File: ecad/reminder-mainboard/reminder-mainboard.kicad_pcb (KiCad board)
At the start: 2 copper layers, 34 parts, among them J1 USB_B_Micro, J2 22-03-5035, J3 22-03-5025, J4 22-03-5065, Q1 2N3904, Q2 2N3904, Q3 2N3904, Q4 2N3904, U1 LM1117-3.3, U2 QRD1113GR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

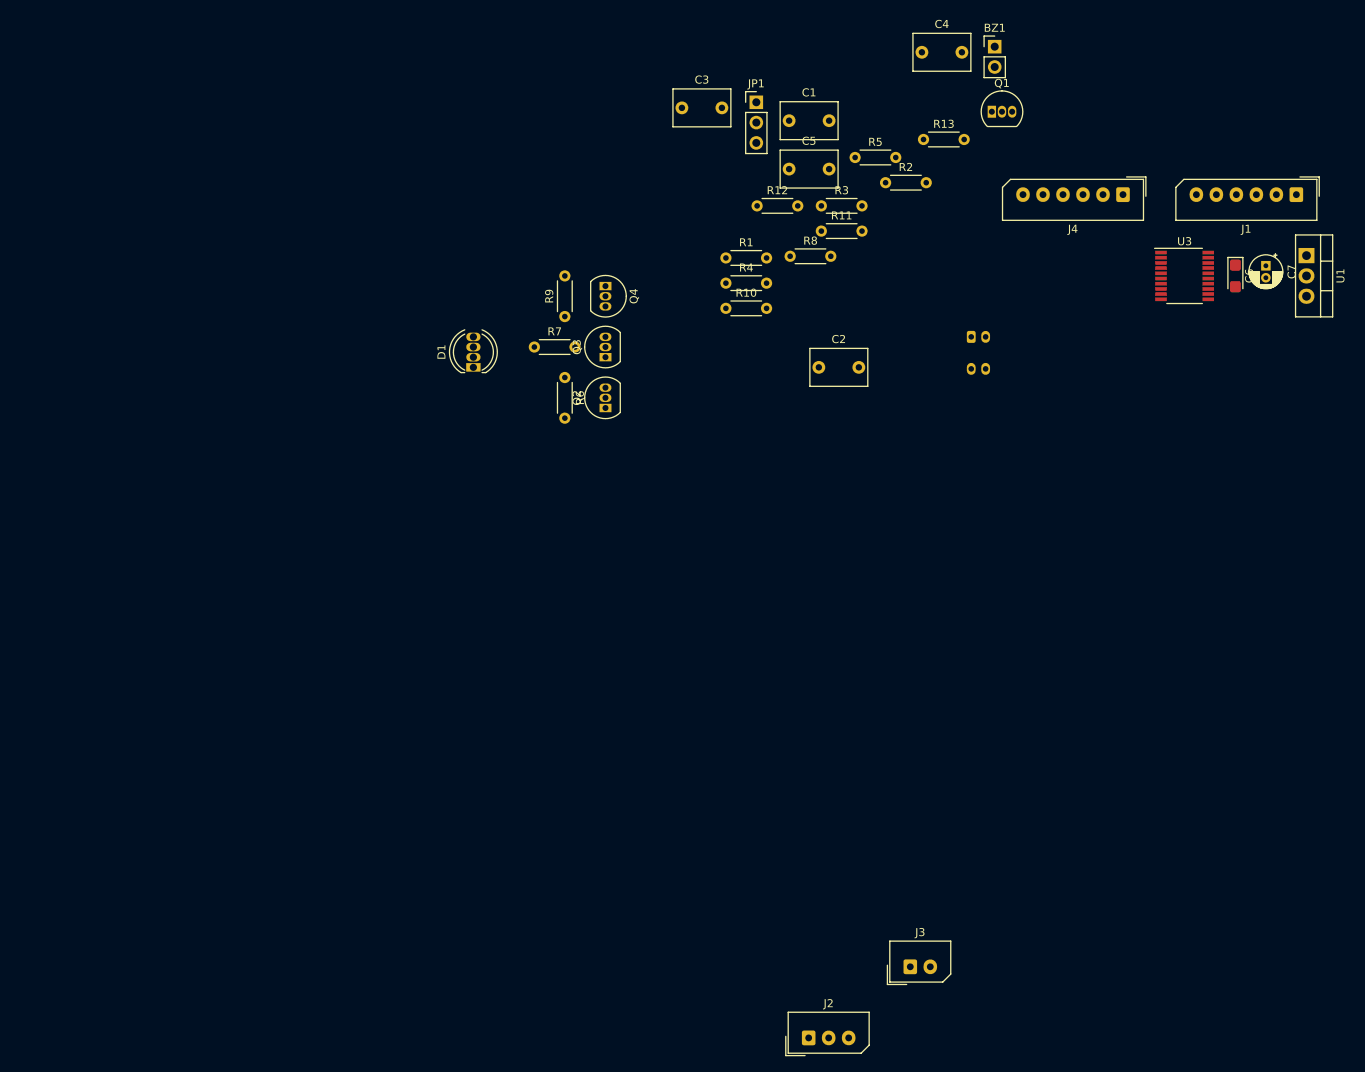
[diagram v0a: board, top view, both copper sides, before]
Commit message: Began SMD layout
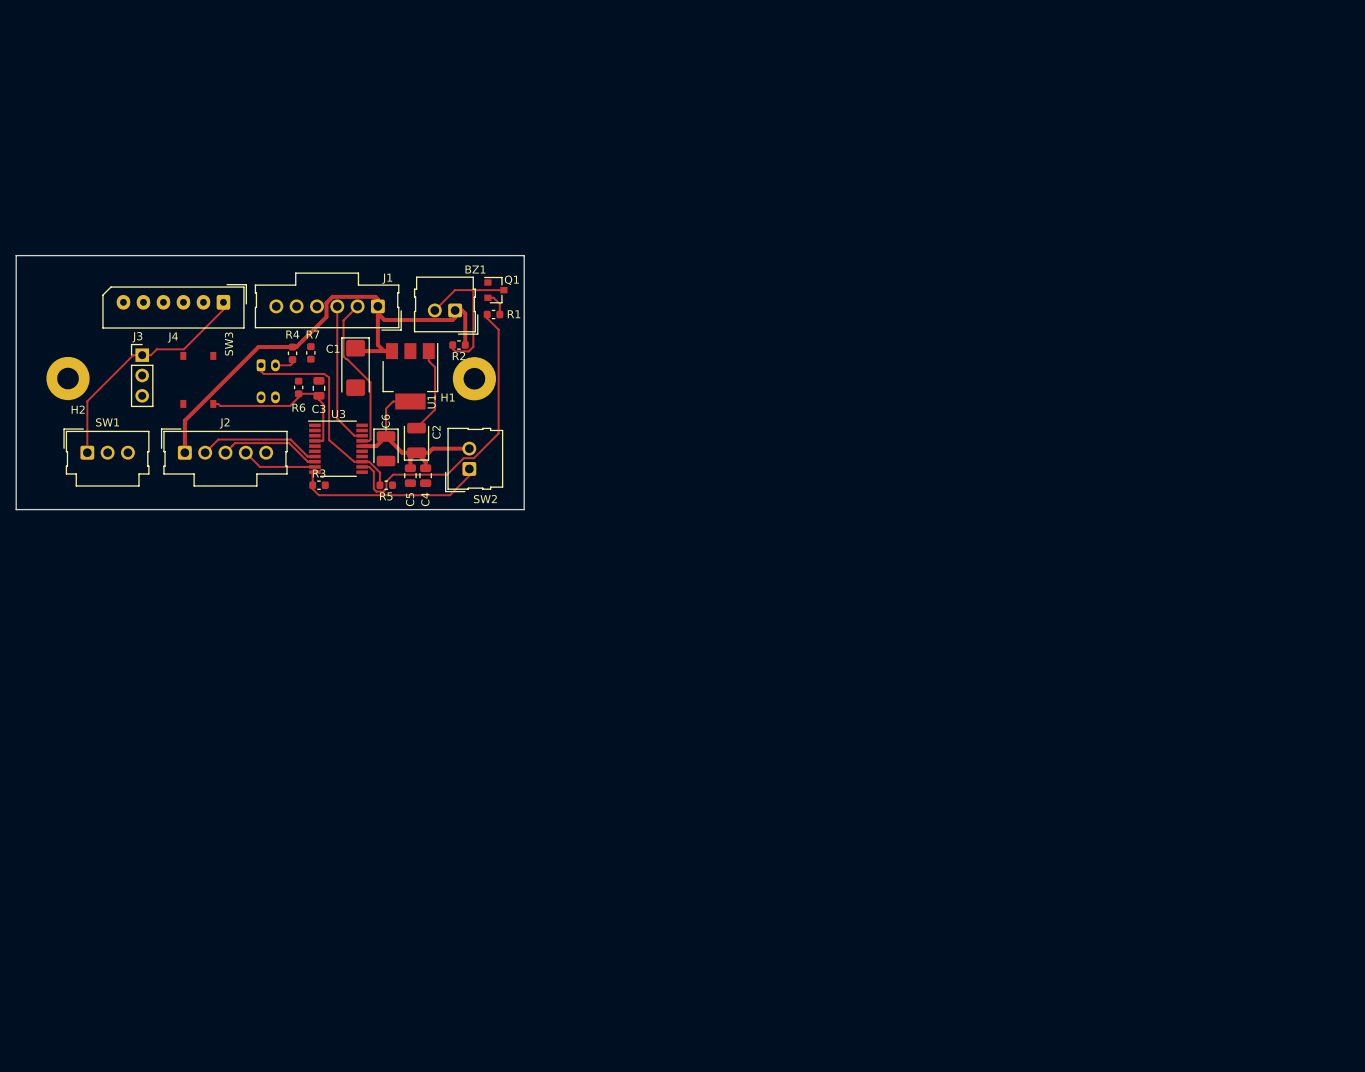
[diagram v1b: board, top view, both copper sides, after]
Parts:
- removed C7: 4.7uF, Capacitor_THT:CP_Radial_D4.0mm_P1.50mm
- removed D1: LED_RGBA, LED_THT:LED_D5.0mm-4_RGB
- removed JP1: Jumper_3_Bridged12, Connector_PinHeader_2.54mm:PinHeader_1x03_P2.54mm_Vertical
- removed Q2, Q3, Q4: 2N3904, Package_TO_SOT_THT:TO-92_Inline
- removed R10: 180, Resistor_THT:R_Axial_DIN0204_L3.6mm_D1.6mm_P5.08mm_Horizontal
- removed R11: 390, Resistor_THT:R_Axial_DIN0204_L3.6mm_D1.6mm_P5.08mm_Horizontal
- removed R12, R13, R8: 10k, Resistor_THT:R_Axial_DIN0204_L3.6mm_D1.6mm_P5.08mm_Horizontal
- removed R9: 91, Resistor_THT:R_Axial_DIN0204_L3.6mm_D1.6mm_P5.08mm_Horizontal
- added H1: MountingHole, MountingHole:MountingHole_2.7mm_M2.5_Pad, F.Cu at (120.8, 110.6)
- added H2: MountingHole, MountingHole:MountingHole_2.7mm_M2.5_Pad, F.Cu at (70.0, 110.6)
- added SW1: SW_SPDT, Connector_Molex:Molex_SL_171971-0003_1x03_P2.54mm_Vertical, F.Cu at (72.4, 119.9)
- added SW2: SW_Push, Connector_Molex:Molex_SL_171971-0002_1x02_P2.54mm_Vertical, F.Cu at (120.1, 121.9)
- added SW3: SW_Push, jlcpcb:TACT_SWITCH_TS-1187A-X-X-X, F.Cu at (88.1, 107.8)
- BZ1: value (none) -> Buzzer; footprint Connector_PinHeader_2.54mm:PinHeader_1x02_P2.54mm_Vertical -> Connector_Molex:Molex_SL_171971-0002_1x02_P2.54mm_Vertical
- C1: footprint Capacitor_THT:C_Rect_L7.0mm_W4.5mm_P5.00mm -> Capacitor_Tantalum_SMD:CP_EIA-6032-28_Kemet-C
- C2: value 10uF -> 100uF; footprint Capacitor_THT:C_Rect_L7.0mm_W4.5mm_P5.00mm -> Capacitor_Tantalum_SMD:CP_EIA-3528-21_Kemet-B
- C3, C4: value 20pF -> 100nF; footprint Capacitor_THT:C_Rect_L7.0mm_W4.5mm_P5.00mm -> Capacitor_SMD:C_0805_2012Metric
- C5: footprint Capacitor_THT:C_Rect_L7.0mm_W4.5mm_P5.00mm -> Capacitor_SMD:C_0805_2012Metric
- C6: value 100nF -> 10uF; footprint Capacitor_Tantalum_SMD:CP_EIA-3216-10_Kemet-I -> Capacitor_Tantalum_SMD:CP_EIA-3528-21_Kemet-B
- J1: footprint Connector_Molex:Molex_SPOX_5267-06A_1x06_P2.50mm_Vertical -> Connector_Molex:Molex_SL_171971-0006_1x06_P2.54mm_Vertical
- J2: value 22-03-5035 -> MOLEX SL 1x5; footprint Connector_Molex:Molex_SPOX_5267-03A_1x03_P2.50mm_Vertical -> Connector_Molex:Molex_SL_171971-0005_1x05_P2.54mm_Vertical
- J3: value 22-03-5025 -> Conn_01x03_Male; footprint Connector_Molex:Molex_SPOX_5267-02A_1x02_P2.50mm_Vertical -> Connector_PinHeader_2.54mm:PinHeader_1x03_P2.54mm_Vertical
- Q1: footprint Package_TO_SOT_THT:TO-92_Inline -> Package_TO_SOT_SMD:SOT-23
- R1: value 620 -> 510; footprint Resistor_THT:R_Axial_DIN0204_L3.6mm_D1.6mm_P5.08mm_Horizontal -> Resistor_SMD:R_0603_1608Metric
- R2: footprint Resistor_THT:R_Axial_DIN0204_L3.6mm_D1.6mm_P5.08mm_Horizontal -> Resistor_SMD:R_0603_1608Metric
- R3, R5: value 620 -> 10k; footprint Resistor_THT:R_Axial_DIN0204_L3.6mm_D1.6mm_P5.08mm_Horizontal -> Resistor_SMD:R_0603_1608Metric
- R4: value 620 -> 160; footprint Resistor_THT:R_Axial_DIN0204_L3.6mm_D1.6mm_P5.08mm_Horizontal -> Resistor_SMD:R_0603_1608Metric
- R6: value 130 -> 10k; footprint Resistor_THT:R_Axial_DIN0204_L3.6mm_D1.6mm_P5.08mm_Horizontal -> Resistor_SMD:R_0603_1608Metric
- R7: value 91 -> 10k; footprint Resistor_THT:R_Axial_DIN0204_L3.6mm_D1.6mm_P5.08mm_Horizontal -> Resistor_SMD:R_0603_1608Metric
- U1: footprint Package_TO_SOT_THT:TO-220-3_Vertical -> Package_TO_SOT_SMD:SOT-223-3_TabPin2
- moved J3 122.7 mm to (79.2, 107.7)
- moved J1 115.7 mm to (108.7, 101.6)
- moved J4 113.2 mm to (89.4, 101.1)
- moved U1 113.0 mm to (112.8, 110.3)
- moved C6 108.3 mm to (109.7, 119.4)
- moved U3 107.9 mm to (103.8, 119.4)
- moved J2 106.9 mm to (84.6, 119.9)
- moved U2 88.8 mm to (94.1, 109.0)
- moved C4 81.5 mm to (114.7, 122.8), turned to 270 degrees
- moved BZ1 75.1 mm to (118.4, 102.1), turned to 180 degrees
- moved R3 71.9 mm to (101.3, 124.0)
- moved R5 71.5 mm to (109.8, 124.0), turned to 180 degrees
- moved Q1 65.9 mm to (123.5, 99.6)
- moved C1 62.4 mm to (105.9, 109.3), turned to 270 degrees
- moved C5 60.9 mm to (112.8, 122.8), turned to 270 degrees
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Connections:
- C3 pad 1: Net-(C3-Pad1) -> /NRST
- C4 pad 1: Net-(C4-Pad1) -> +3V3
- C5 pad 1: /NRST -> +3V3
- J2 pad 1: +3V3 -> +5V
- J2 pad 2: /MUTE -> /LED_R
- J2 pad 3: GND -> /LED_G
- J3 pad 2: /UI_BUTTON -> Net-(J3-Pad2)
- R3 pad 1: /LED_R -> /UI_BUTTON
- R3 pad 2: Net-(Q2-Pad2) -> GND
- R4 pad 1: /LED_G -> +5V
- R4 pad 2: Net-(Q3-Pad2) -> Net-(R4-Pad2)
- R5 pad 1: /LED_B -> +3V3
- R5 pad 2: Net-(Q4-Pad2) -> /SENSOR
- R6 pad 1: Net-(D1-Pad1) -> +3V3
- R6 pad 2: Net-(Q2-Pad3) -> /NRST
- R7 pad 1: Net-(D1-Pad2) -> Net-(R7-Pad1)
- R7 pad 2: Net-(Q3-Pad3) -> Net-(J3-Pad2)
- U2 pad 3: Net-(R10-Pad2) -> Net-(R4-Pad2)
- U3 pad 1: Net-(R13-Pad1) -> Net-(R7-Pad1)
- U3 pad 2: Net-(C3-Pad1) -> (no net)
- U3 pad 3: Net-(R11-Pad1) -> (no net)
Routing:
- net +5V: track 0.00 -> 65.4 mm
- net +3V3: track 0.00 -> 55.6 mm
- net /BUZZER: track 0.00 -> 38.6 mm
- net /SENSOR: track 0.00 -> 26.9 mm
- net /UI_BUTTON: track 0.00 -> 24.0 mm
- net /NRST: track 0.00 -> 21.2 mm
- net Net-(BZ1-Pad2): track 0.00 -> 20.2 mm
- net /USB_M: track 0.00 -> 20.0 mm
- net /USB_P: track 0.00 -> 18.0 mm
- net /LED_R: track 0.00 -> 15.3 mm
- net /LED_G: track 0.00 -> 12.6 mm
- net GND: track 0.00 -> 10.9 mm
- net /LED_B: track 0.00 -> 9.37 mm
- net Net-(Q1-Pad2): track 0.00 -> 3.13 mm
- net Net-(R4-Pad2): track 0.00 -> 2.69 mm
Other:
- board outline added: 63.5 x 31.8 mm

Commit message: Finished routing
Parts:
- moved R5 5.11 mm to (104.6, 124.0), turned to 0 degrees
- moved R3 1.06 mm to (100.6, 124.7), turned to 270 degrees
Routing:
- net +3V3: track 55.6 -> 101.8 mm, vias 0 -> 2
- net /SWDIO: track 0.00 -> 38.1 mm, vias 0 -> 1
- net /MUTE: track 0.00 -> 35.4 mm, vias 0 -> 2
- net GND: track 10.9 -> 40.3 mm, vias 0 -> 11
- net /SWCLK: track 0.00 -> 28.5 mm, vias 0 -> 1
- net Net-(J3-Pad2): track 0.00 -> 24.2 mm, vias 0 -> 2
- net /NRST: track 21.2 -> 40.2 mm, vias 0 -> 1
- net Net-(R7-Pad1): track 0.00 -> 8.96 mm, vias 0 -> 2
- net /SENSOR: track 26.9 -> 32.3 mm, vias 0 -> 2
- net +5V: track 65.4 -> 70.1 mm
- net /BUZZER: track 38.6 -> 37.7 mm
- added copper zone on B.Cu, net GND
